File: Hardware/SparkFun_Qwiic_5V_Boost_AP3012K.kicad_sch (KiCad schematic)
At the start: 35 parts, among them J1 Qwiic_RA, J2 Qwiic_RA, J3 Conn_01x06, Q1 BSS138, Q2 BSS138, U1 AP3012

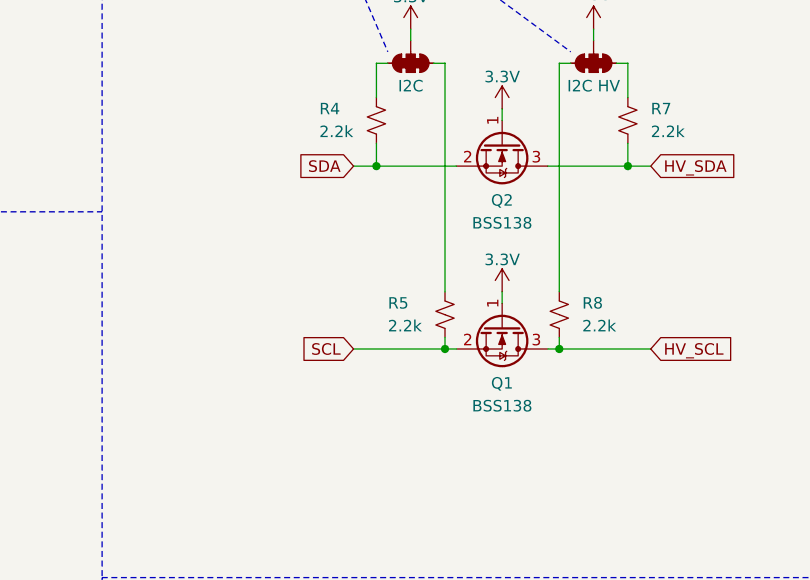
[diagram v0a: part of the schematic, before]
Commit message: added 2 test points
-added test points for 3V3 logic level SDA/SCL
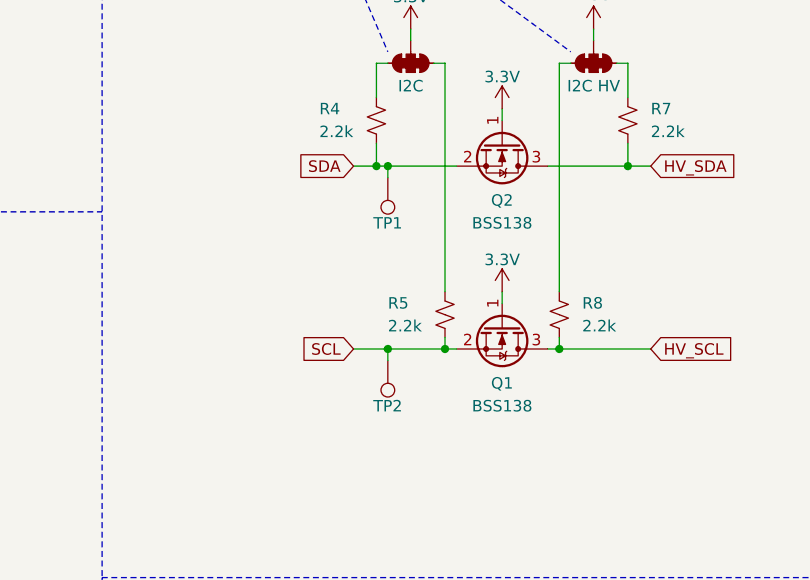
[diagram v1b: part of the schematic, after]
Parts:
- added TP1, TP2: 1.0mm, SparkFun-Connector:TestPoint-1.0mm, symbol SparkFun-Connector:TestPoint_1.0mm
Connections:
- net SCL: now also TP2.1
- net SDA: now also TP1.1
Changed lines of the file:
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@@
 	)
 	(junction
+		(at 187.96 99.06)
+		(diameter 0)
+		(color 0 0 0 0)
+	)
+	(junction
 		(at 33.02 33.02)
 		(diameter 0)
@@
 	)
 	(junction
+		(at 187.96 78.74)
+		(diameter 0)
+		(color 0 0 0 0)
+	)
+	(junction
 		(at 186.69 78.74)
 		(diameter 0)
@@
 	(wire
 		(pts
+			(xy 187.96 99.06) (xy 187.96 100.33)
+		)
+		(stroke
+			(width 0)
+			(type default)
+		)
+	)
+	(wire
+		(pts
 			(xy 57.15 46.99) (xy 67.31 46.99)
 		)
@@
 	(wire
 		(pts
+			(xy 187.96 78.74) (xy 187.96 80.01)
+		)
+		(stroke
+			(width 0)
+			(type default)
+		)
+	)
+	(wire
+		(pts
 			(xy 120.65 168.91) (xy 120.65 175.26)
 		)
@@
 	(wire
 		(pts
-			(xy 186.69 78.74) (xy 195.58 78.74)
+			(xy 186.69 78.74) (xy 187.96 78.74)
 		)
 		(stroke
@@
 	(wire
 		(pts
+			(xy 187.96 78.74) (xy 195.58 78.74)
+		)
+		(stroke
+			(width 0)
+			(type default)
+		)
+	)
+	(wire
+		(pts
 			(xy 124.46 182.88) (xy 115.57 182.88)
 		)
@@
 	(wire
 		(pts
+			(xy 187.96 99.06) (xy 194.31 99.06)
+		)
+		(stroke
+			(width 0)
+			(type default)
+		)
+	)
+	(wire
+		(pts
 			(xy 33.02 33.02) (xy 33.02 36.83)
 		)
@@
 	(wire
 		(pts
-			(xy 184.15 99.06) (xy 194.31 99.06)
+			(xy 184.15 99.06) (xy 187.96 99.06)
 		)
 		(stroke
@@
 	)
 	(symbol
+		(lib_id "SparkFun-Connector:TestPoint_1.0mm")
+		(at 187.96 80.01 180)
+		(unit 1)
+		(exclude_from_sim no)
+		(in_bom yes)
+		(on_board yes)
+		(dnp no)
+		(fields_autoplaced yes)
+		(property "Reference" "TP1"
+			(at 187.96 85.09 0)
+			(do_not_autoplace yes)
+			(effects
+				(font
+					(size 1.27 1.27)
+				)
+			)
+		)
+		(property "Value" "1.0mm"
+			(at 187.96 76.2 0)
+			(effects
+				(font
+					(size 1.27 1.27)
+				)
+				(hide yes)
+			)
+		)
+		(property "Footprint" "SparkFun-Connector:TestPoint-1.0mm"
+			(at 187.96 73.66 0)
+			(effects
+				(font
+					(size 1.27 1.27)
+				)
+				(hide yes)
+			)
+		)
+		(property "Datasheet" "~"
+			(at 187.96 72.39 0)
+			(effects
+				(font
+					(size 1.27 1.27)
+				)
+				(hide yes)
+			)
+		)
+		(property "Description" "Test Point"
+			(at 187.96 69.85 0)
+			(effects
+				(font
+					(size 1.27 1.27)
+				)
+				(hide yes)
+			)
+		)
+		(pin "1"
+		)
+		(instances
+			(project ""
+				(path "/e3dd3ae4-244d-4cba-9cca-5d2abf83f29a"
+					(reference "TP1")
+					(unit 1)
+				)
+			)
+		)
+	)
+	(symbol
 		(lib_id "SparkFun-PowerSymbol:GND")
 		(at 77.47 53.34 0)
@@
 					(unit 1)
 				)
+			)
+		)
+	)
+	(symbol
+		(lib_id "SparkFun-Connector:TestPoint_1.0mm")
+		(at 187.96 100.33 180)
+		(unit 1)
+		(exclude_from_sim no)
+		(in_bom yes)
+		(on_board yes)
+		(dnp no)
+		(fields_autoplaced yes)
+		(property "Reference" "TP2"
+			(at 187.96 105.41 0)
+			(do_not_autoplace yes)
+			(effects
+				(font
+					(size 1.27 1.27)
+				)
+			)
+		)
+		(property "Value" "1.0mm"
+			(at 187.96 96.52 0)
+			(effects
+				(font
+					(size 1.27 1.27)
+				)
+				(hide yes)
+			)
+		)
+		(property "Footprint" "SparkFun-Connector:TestPoint-1.0mm"
+			(at 187.96 93.98 0)
+			(effects
+				(font
+					(size 1.27 1.27)
+				)
+				(hide yes)
+			)
+		)
+		(property "Datasheet" "~"
+			(at 187.96 92.71 0)
+			(effects
+				(font
+					(size 1.27 1.27)
+				)
+				(hide yes)
+			)
+		)
+		(property "Description" "Test Point"
+			(at 187.96 90.17 0)
+			(effects
+				(font
+					(size 1.27 1.27)
+				)
+				(hide yes)
+			)
+		)
+		(pin "1"
+		)
+		(instances
+			(project ""
+				(path "/e3dd3ae4-244d-4cba-9cca-5d2abf83f29a"
+					(reference "TP2")
+					(unit 1)
+				)
